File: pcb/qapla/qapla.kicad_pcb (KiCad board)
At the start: 2 copper layers, 154.4 x 126.1 mm, 72 parts

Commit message: Adjusting hole positions
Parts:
- removed MH3, MH4, MH5, MH6, MH7: , ceoloide:mounting_hole_npth
- removed the _3 at (232.4, 76.8) (x2)
- added H1: , ceoloide:mounting_hole_plated, F.Cu at (137.8, 44.6)
- added H2: , ceoloide:mounting_hole_plated, F.Cu at (157.7, 109.2)
- added H3: , ceoloide:mounting_hole_plated, F.Cu at (211.8, 33.5)
- added H4: , ceoloide:mounting_hole_plated, F.Cu at (211.9, 108.3)
- added H5: , ceoloide:mounting_hole_plated, F.Cu at (243.5, 99.0)
- added _3: , D_0805_2012Metric_Pad1.15x1.40mm_HandSolder, F.Cu at (232.4, 76.8)
- added _3: , R_0805_2012Metric_Pad1.20x1.40mm_HandSolder, F.Cu at (232.4, 76.8)
- _1: footprint trrs_jumper -> reset_switch
- moved MH1 94.7 mm to (225.4, 84.7), turned to 0 degrees
- moved MH2 93.2 mm to (247.9, 84.7), turned to 0 degrees
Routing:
- net (no net): track 0.00 -> 337.7 mm
- net VCC: track 59.3 -> 0.00 mm
- net RST: track 40.4 -> 0.00 mm
- net GND: track 29.5 -> 0.00 mm
- net RAW: track 25.5 -> 0.00 mm
- net BAT_P: track 14.0 -> 0.00 mm
- net P10: track 9.84 -> 0.00 mm
- net P21: track 9.84 -> 0.00 mm
- net P20: track 9.84 -> 0.00 mm
- net P19: track 9.84 -> 0.00 mm
- net P18: track 9.84 -> 0.00 mm
- net P16: track 9.84 -> 0.00 mm
- net P15: track 9.84 -> 0.00 mm
- net P14: track 9.84 -> 0.00 mm
- net P8: track 9.83 -> 0.00 mm
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
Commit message: Starting work on bottom case
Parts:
- moved H3 4.58 mm to (207.3, 32.7)
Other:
- outline, holes or cut-outs redrawn
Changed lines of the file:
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@@
       (effects (font (size 1 1) (thickness 0.15)))
     )
-    (pad "" thru_hole circle (at 0 0 0) (size 3.8 3.8) (drill 3.4) (layers "*.Cu" "*.Mask"))
-    (fp_circle (center 0 0) (end -2.15 0) (layer "F.CrtYd") (stroke (width 0.05) (type solid)) (fill none))
-    (fp_circle (center 0 0) (end -2.15 0) (layer "B.CrtYd") (stroke (width 0.05) (type solid)) (fill none))
+    (pad "" thru_hole circle (at 0 0 0) (size 5.4 5.4) (drill 5) (layers "*.Cu" "*.Mask"))
+    (fp_circle (center 0 0) (end -2.95 0) (layer "F.CrtYd") (stroke (width 0.05) (type solid)) (fill none))
+    (fp_circle (center 0 0) (end -2.95 0) (layer "B.CrtYd") (stroke (width 0.05) (type solid)) (fill none))
   )
   (footprint "ceoloide:mounting_hole_plated"
@@
       (effects (font (size 1 1) (thickness 0.15)))
     )
-    (pad "" thru_hole circle (at 0 0 0) (size 3.8 3.8) (drill 3.4) (layers "*.Cu" "*.Mask"))
-    (fp_circle (center 0 0) (end -2.15 0) (layer "F.CrtYd") (stroke (width 0.05) (type solid)) (fill none))
-    (fp_circle (center 0 0) (end -2.15 0) (layer "B.CrtYd") (stroke (width 0.05) (type solid)) (fill none))
+    (pad "" thru_hole circle (at 0 0 0) (size 5.4 5.4) (drill 5) (layers "*.Cu" "*.Mask"))
+    (fp_circle (center 0 0) (end -2.95 0) (layer "F.CrtYd") (stroke (width 0.05) (type solid)) (fill none))
+    (fp_circle (center 0 0) (end -2.95 0) (layer "B.CrtYd") (stroke (width 0.05) (type solid)) (fill none))
   )
   (footprint "ceoloide:mounting_hole_plated"
     (layer "F.Cu")
-    (at 211.8 33.55 0)
+    (at 207.3 32.7 0)
     (property "Reference" "H3"
       (at 0 3 0)
@@
       (effects (font (size 1 1) (thickness 0.15)))
     )
-    (pad "" thru_hole circle (at 0 0 0) (size 3.8 3.8) (drill 3.4) (layers "*.Cu" "*.Mask"))
-    (fp_circle (center 0 0) (end -2.15 0) (layer "F.CrtYd") (stroke (width 0.05) (type solid)) (fill none))
-    (fp_circle (center 0 0) (end -2.15 0) (layer "B.CrtYd") (stroke (width 0.05) (type solid)) (fill none))
+    (pad "" thru_hole circle (at 0 0 0) (size 5.4 5.4) (drill 5) (layers "*.Cu" "*.Mask"))
+    (fp_circle (center 0 0) (end -2.95 0) (layer "F.CrtYd") (stroke (width 0.05) (type solid)) (fill none))
+    (fp_circle (center 0 0) (end -2.95 0) (layer "B.CrtYd") (stroke (width 0.05) (type solid)) (fill none))
   )
   (footprint "ceoloide:mounting_hole_plated"
@@
       (effects (font (size 1 1) (thickness 0.15)))
     )
-    (pad "" thru_hole circle (at 0 0 0) (size 3.8 3.8) (drill 3.4) (layers "*.Cu" "*.Mask"))
-    (fp_circle (center 0 0) (end -2.15 0) (layer "F.CrtYd") (stroke (width 0.05) (type solid)) (fill none))
-    (fp_circle (center 0 0) (end -2.15 0) (layer "B.CrtYd") (stroke (width 0.05) (type solid)) (fill none))
+    (pad "" thru_hole circle (at 0 0 0) (size 5.4 5.4) (drill 5) (layers "*.Cu" "*.Mask"))
+    (fp_circle (center 0 0) (end -2.95 0) (layer "F.CrtYd") (stroke (width 0.05) (type solid)) (fill none))
+    (fp_circle (center 0 0) (end -2.95 0) (layer "B.CrtYd") (stroke (width 0.05) (type solid)) (fill none))
   )
   (footprint "ceoloide:mounting_hole_plated"
@@
       (effects (font (size 1 1) (thickness 0.15)))
     )
-    (pad "" thru_hole circle (at 0 0 0) (size 3.8 3.8) (drill 3.4) (layers "*.Cu" "*.Mask"))
-    (fp_circle (center 0 0) (end -2.15 0) (layer "F.CrtYd") (stroke (width 0.05) (type solid)) (fill none))
-    (fp_circle (center 0 0) (end -2.15 0) (layer "B.CrtYd") (stroke (width 0.05) (type solid)) (fill none))
+    (pad "" thru_hole circle (at 0 0 0) (size 5.4 5.4) (drill 5) (layers "*.Cu" "*.Mask"))
+    (fp_circle (center 0 0) (end -2.95 0) (layer "F.CrtYd") (stroke (width 0.05) (type solid)) (fill none))
+    (fp_circle (center 0 0) (end -2.95 0) (layer "B.CrtYd") (stroke (width 0.05) (type solid)) (fill none))
   )
   (gr_line (start 112.41612146766047 122.13354750570238) (end 100.99025906060282 57.33426183375843) (layer Edge.Cuts) (stroke (width 0.15) (type default)))
@@
 (gr_line (start 165.2052490631292 27.7375409) (end 206.42089269436943 27.7375409) (layer Edge.Cuts) (stroke (width 0.15) (type default)))
 (gr_line (start 207.31531989436945 27.948686499999994) (end 221.47073750563055 35.0263954) (layer Edge.Cuts) (stroke (width 0.15) (type default)))
-(gr_line (start 251.3930287 108.57235164136341) (end 251.3930287 37.237541) (layer Edge.Cuts) (stroke (width 0.15) (type default)))
+(gr_line (start 251.3930287 108.57235164136341) (end 251.3930287 55.237541) (layer Edge.Cuts) (stroke (width 0.15) (type default)))
+(gr_line (start 251.3930287 53.237541) (end 251.3930287 37.237541) (layer Edge.Cuts) (stroke (width 0.15) (type default)))
 (gr_line (start 251.42013130000004 108.90049164136349) (end 255.34141913312294 132.47670792711529) (layer Edge.Cuts) (stroke (width 0.15) (type default)))
 (gr_line (start 254.9006105918054 134.09042317635573) (end 238.89097308266068 153.16996618545056) (layer Edge.Cuts) (stroke (width 0.15) (type default)))
@@
 (gr_arc (start 236.3081217 153.5861248) (mid 237.6770285 153.8589249) (end 238.8909731 153.1699663) (layer Edge.Cuts) (stroke (width 0.15) (type default)))
 (gr_arc (start 112.4161216 122.13354749999999) (mid 113.1570006 123.36428989999999) (end 114.5317935 123.78091089999998) (layer Edge.Cuts) (stroke (width 0.15) (type default)))
+(gr_line (start 247.8930287 55.237541) (end 251.3930287 55.237541) (layer Edge.Cuts) (stroke (width 0.15) (type default)))
+(gr_line (start 251.3930287 53.237541) (end 247.8930287 53.237541) (layer Edge.Cuts) (stroke (width 0.15) (type default)))
+(gr_line (start 247.8930287 53.237541) (end 247.8930287 55.237541) (layer Edge.Cuts) (stroke (width 0.15) (type default)))
 (gr_line (start 114.3915125 123.2586989) (end 131.6256482 120.21985579999999) (layer Eco1.User) (stroke (width 0.15) (type default)))
 (gr_line (start 131.6256482 120.21985579999999) (end 128.7604533 103.9705279) (layer Eco1.User) (stroke (width 0.15) (type default)))

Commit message: Finalising Plate and PCB design for choc
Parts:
- removed the _3 at (232.4, 76.8) (x2)
- added _3: , D_0805_2012Metric_Pad1.15x1.40mm_HandSolder, F.Cu at (232.2, 77.2)
- added _3: , R_0805_2012Metric_Pad1.20x1.40mm_HandSolder, F.Cu at (232.2, 77.2)
- moved D16 0.47 mm to (139.3, 68.7)
- moved H5 0.47 mm to (243.3, 99.4)
- moved S9 0.47 mm to (156.2, 95.8)
- moved S1 0.47 mm to (121.3, 114.0)
- moved D11 0.47 mm to (218.7, 87.1)
- moved DISP1 0.47 mm to (232.2, 57.6)
- moved D7 0.47 mm to (182.7, 79.6)
- moved D28 0.47 mm to (218.7, 116.1)
- moved JST1 0.47 mm to (245.9, 44.6)
- moved D8 0.47 mm to (182.7, 45.6)
- moved S11 0.47 mm to (153.2, 61.9)
- moved D20 0.47 mm to (182.7, 81.6)
- moved S16 0.47 mm to (175.2, 55.1)
- moved S19 0.47 mm to (193.2, 77.1)
- moved D19 0.47 mm to (182.7, 98.6)
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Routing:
- net (no net): track 337.7 -> 0.00 mm
- net P9: track 0.00 -> 134.4 mm, vias 0 -> 2
- net P8: track 0.00 -> 133.2 mm, vias 0 -> 2
- net P7: track 0.00 -> 128.1 mm, vias 0 -> 2
- net P6: track 0.00 -> 127.6 mm, vias 0 -> 2
- net P19: track 0.00 -> 99.1 mm
- net P18: track 0.00 -> 87.7 mm
- net P15: track 0.00 -> 77.8 mm
- net P10: track 0.00 -> 60.8 mm
- net P16: track 0.00 -> 60.8 mm
- net P14: track 0.00 -> 60.8 mm
- net P20: track 0.00 -> 55.5 mm
- net GND: track 0.00 -> 29.5 mm
- net inner_home: track 0.00 -> 12.0 mm
- net index_home: track 0.00 -> 12.0 mm
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
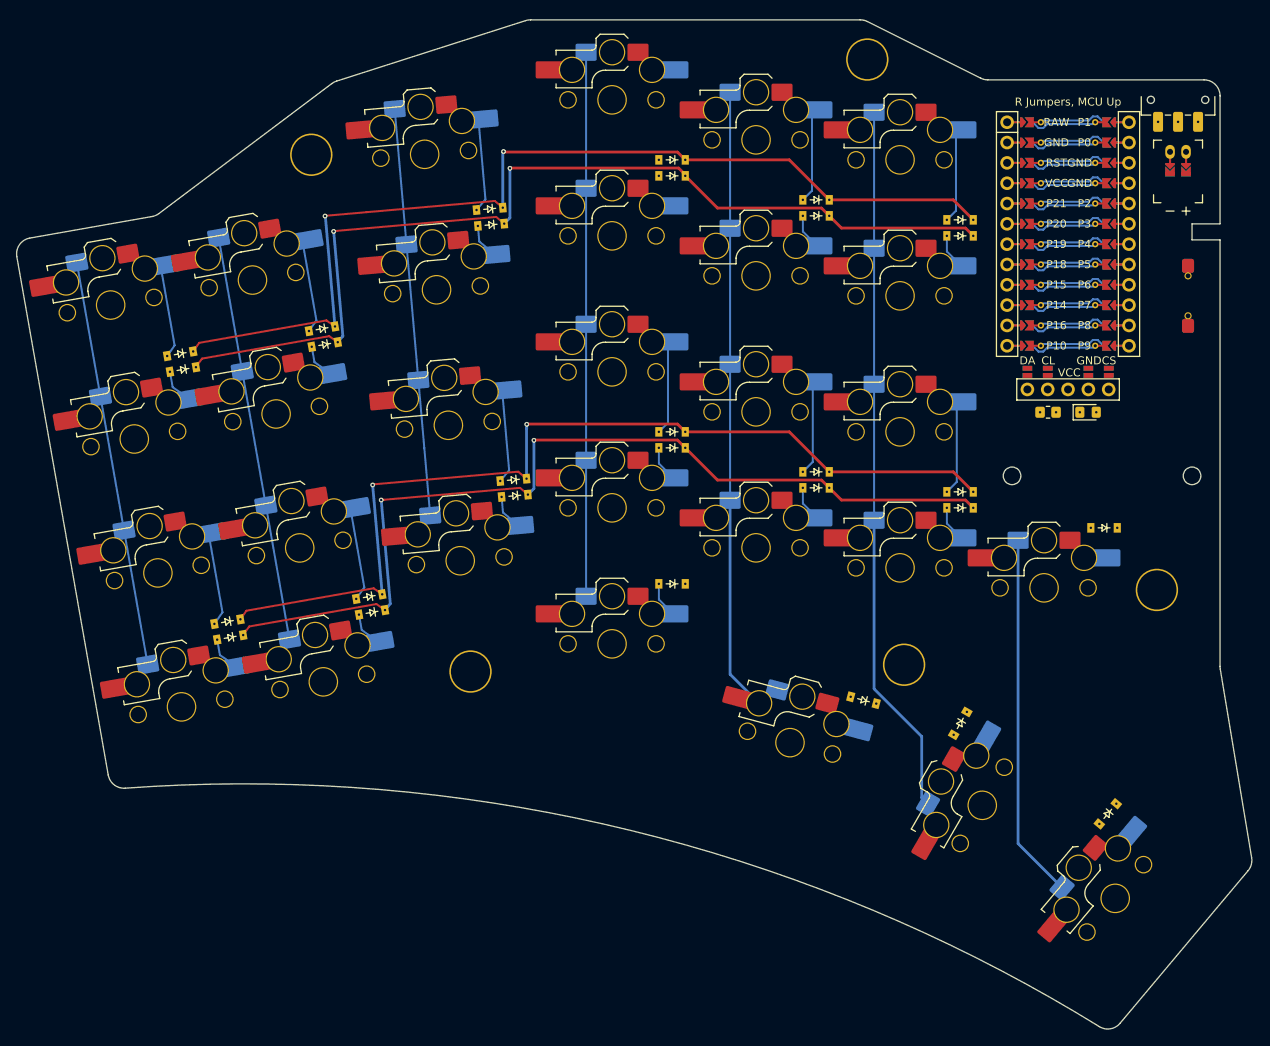
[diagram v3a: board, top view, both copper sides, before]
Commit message: Adjusting distance between diodes to accomodate traces
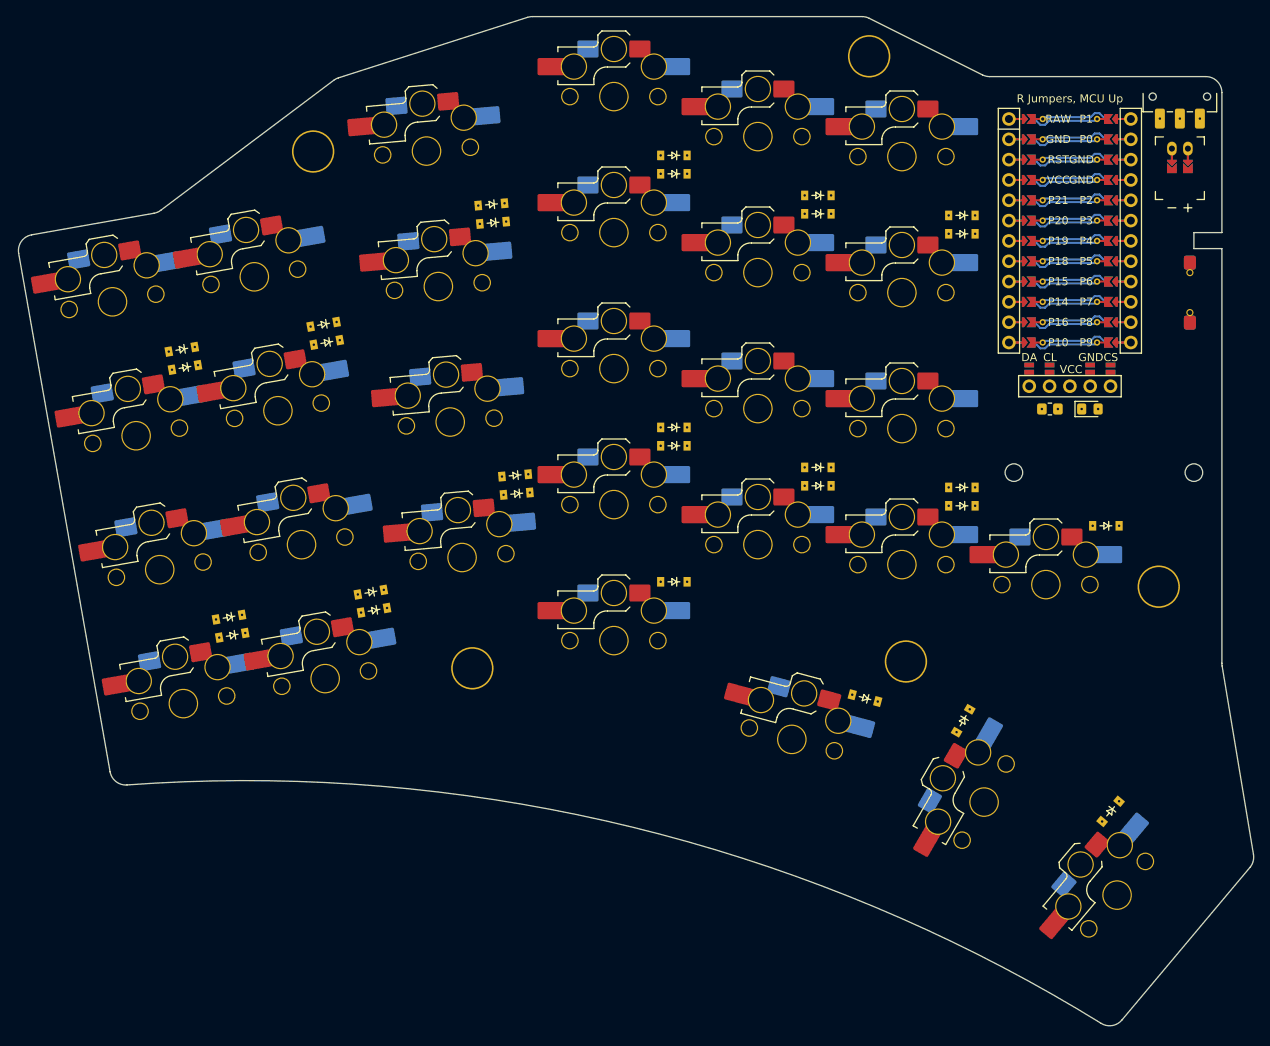
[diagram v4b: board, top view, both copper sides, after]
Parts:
- removed the _3 at (232.2, 77.2) (x2)
- added _3: , D_0805_2012Metric_Pad1.15x1.40mm_HandSolder, F.Cu at (232.4, 76.8)
- added _3: , R_0805_2012Metric_Pad1.20x1.40mm_HandSolder, F.Cu at (232.4, 76.8)
- moved D11 0.60 mm to (218.9, 86.6)
- moved D8 0.60 mm to (182.9, 45.1)
- moved D7 0.60 mm to (182.9, 79.1)
- moved D9 0.60 mm to (200.9, 84.1)
- moved D10 0.60 mm to (200.9, 50.1)
- moved D12 0.60 mm to (218.9, 52.6)
- moved D5 0.60 mm to (163.0, 85.1)
- moved D6 0.60 mm to (160.1, 51.2)
- moved D4 0.59 mm to (139.1, 66.2)
- moved D2 0.59 mm to (121.4, 69.3)
- moved D1 0.59 mm to (127.3, 102.8)
- moved D3 0.59 mm to (145.0, 99.7)
- moved D28 0.49 mm to (219.1, 115.8)
- moved H5 0.47 mm to (243.5, 99.0)
- moved S9 0.47 mm to (156.4, 95.4)
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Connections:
- D27 pad 1: P9 -> P5
- D28 pad 1: P9 -> P5
- D29 pad 1: P9 -> P5
- S1 pad 1: P10 -> P20
- S10 pad 1: P14 -> P18
- S11 pad 1: P14 -> P18
- S12 pad 1: P14 -> P18
- S18 pad 1: P18 -> P14
- S19 pad 1: P18 -> P14
- S2 pad 1: P10 -> P20
- S20 pad 1: P18 -> P14
- S21 pad 1: P18 -> P14
- S22 pad 1: P19 -> P16
- S23 pad 1: P19 -> P16
- S24 pad 1: P19 -> P16
- S25 pad 1: P19 -> P16
- S26 pad 1: P20 -> P10
- S27 pad 1: P18 -> P14
- S28 pad 1: P19 -> P16
- S29 pad 1: P20 -> P10
- S3 pad 1: P10 -> P20
- S4 pad 1: P10 -> P20
- S5 pad 1: P16 -> P19
- S6 pad 1: P16 -> P19
- S7 pad 1: P16 -> P19
- S8 pad 1: P16 -> P19
- S9 pad 1: P14 -> P18
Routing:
- net (no net): track 0.00 -> 337.7 mm
- net P9: track 134.4 -> 0.00 mm, vias 2 -> 0
- net P8: track 133.2 -> 0.00 mm, vias 2 -> 0
- net P7: track 128.1 -> 0.00 mm, vias 2 -> 0
- net P6: track 127.6 -> 0.00 mm, vias 2 -> 0
- net P19: track 99.1 -> 0.00 mm
- net P18: track 87.7 -> 0.00 mm
- net P15: track 77.8 -> 0.00 mm
- net P10: track 60.8 -> 0.00 mm
- net P16: track 60.8 -> 0.00 mm
- net P14: track 60.8 -> 0.00 mm
- net P20: track 55.5 -> 0.00 mm
- net GND: track 29.5 -> 0.00 mm
- net inner_home: track 12.0 -> 0.00 mm
- net index_home: track 12.0 -> 0.00 mm
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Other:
- outline, holes or cut-outs redrawn
